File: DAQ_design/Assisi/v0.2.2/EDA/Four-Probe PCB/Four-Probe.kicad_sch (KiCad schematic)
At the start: 6 parts, among them J1 7-POS Plug Terminal, J2 Two-Probe Measurement, J3 7-POS Plug Terminal, J4 Four-Probe Measurement

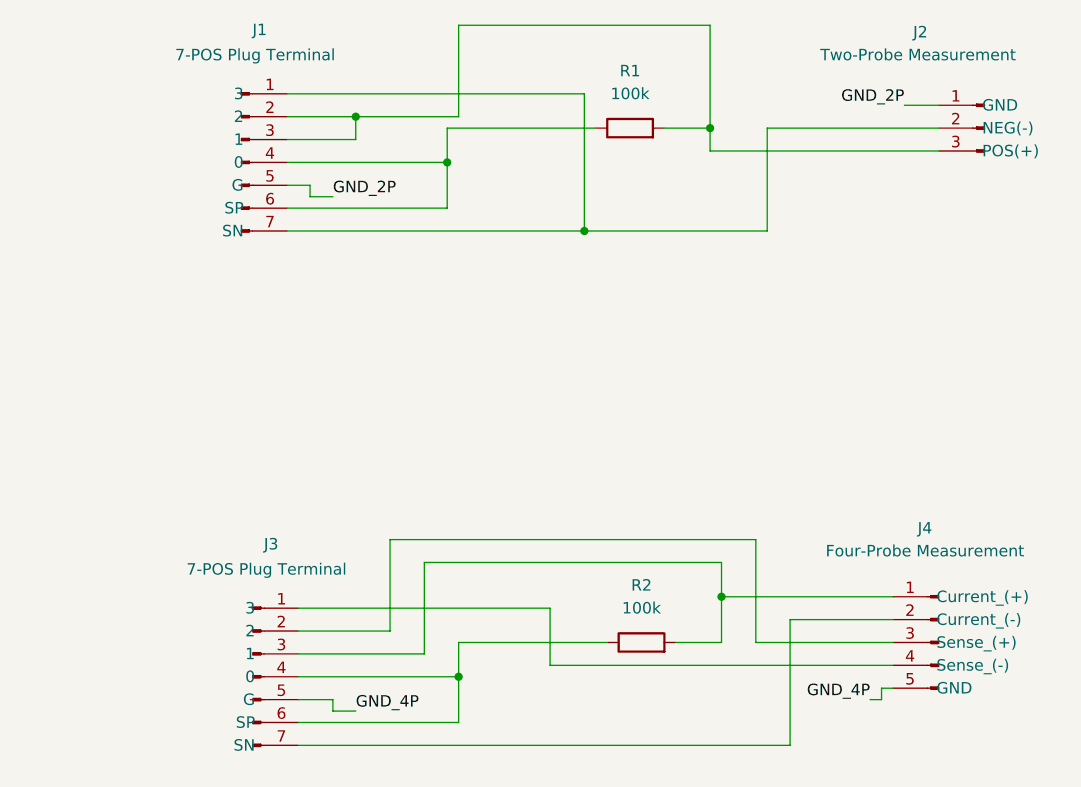
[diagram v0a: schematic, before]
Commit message: Separated PCBs: Two-Probe and Four-Probe
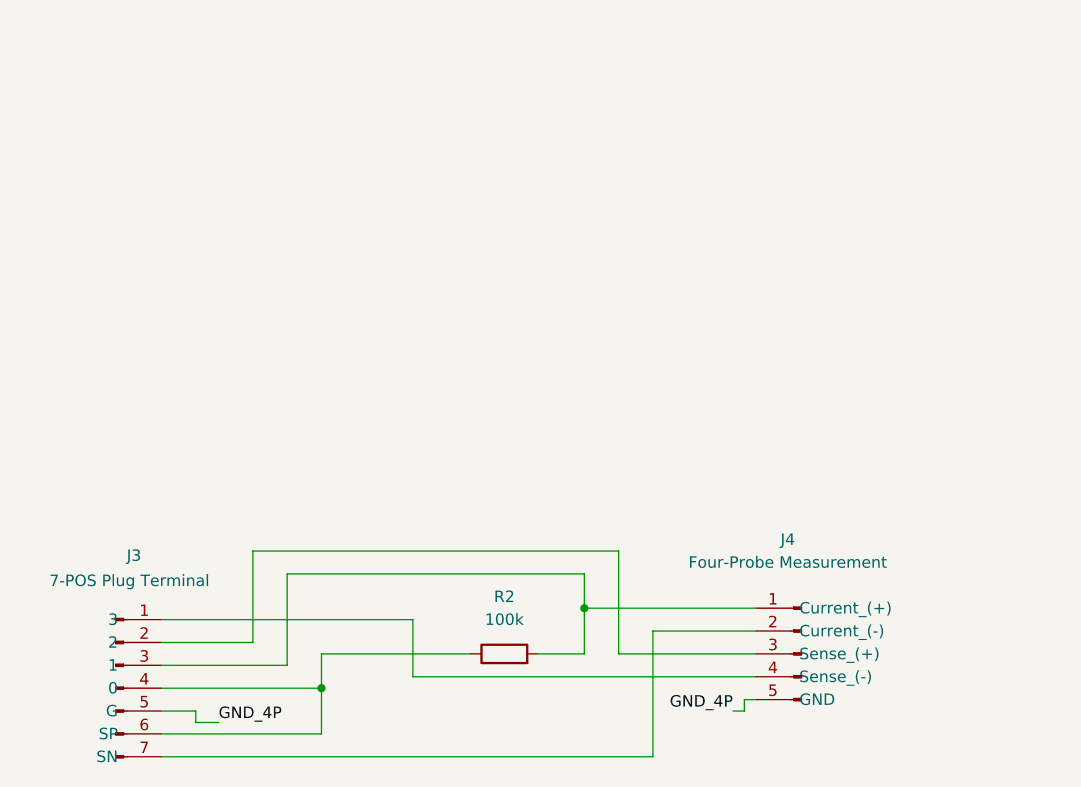
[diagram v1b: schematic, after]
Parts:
- removed J1: 7-POS Plug Terminal, EDA Footprint:PHOENIX_1786459, symbol Connector:Conn_01x07_Pin
- removed J2: Two-Probe Measurement, Connector_Phoenix_MSTB:PhoenixContact_MSTBA_2,5_3-G-5,08_1x03_P5.08mm_Horizontal, symbol Connector:Conn_01x03_Pin
- removed R1: 100k, Resistor_THT:R_Axial_DIN0207_L6.3mm_D2.5mm_P10.16mm_Horizontal, symbol Device:R
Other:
- moved on the sheet: J3, J4, R2
